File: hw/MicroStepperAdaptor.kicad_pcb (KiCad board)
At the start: 2 copper layers, 23 x 18 mm, 9 parts, among them P1 CONN_6, U1 QSBT40, U2 2_Phase_Motor

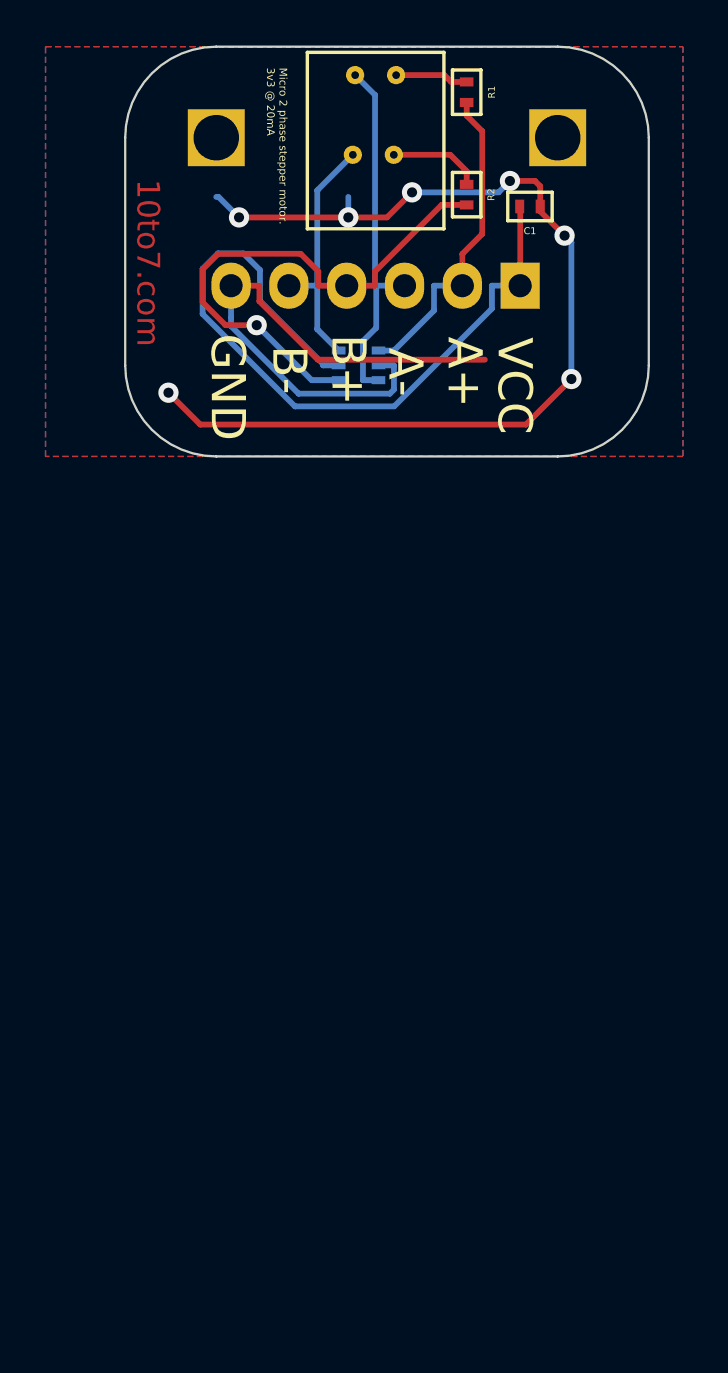
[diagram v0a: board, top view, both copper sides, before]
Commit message: revised stepper motor footprint and reduced the size of the board.
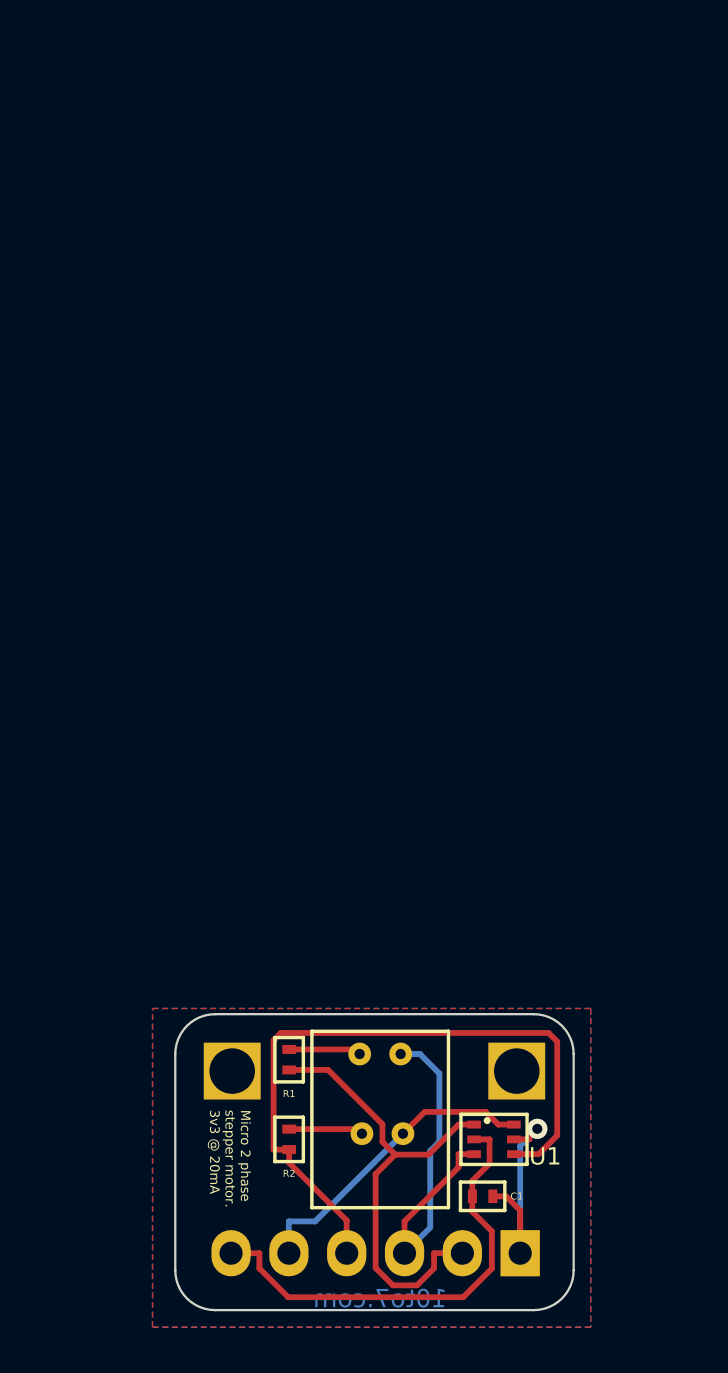
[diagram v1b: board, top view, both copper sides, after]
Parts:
- U1: moved to F.Cu
- U2: moved to B.Cu
- moved C1 43.5 mm to (146.7, 151.5), turned to 180 degrees
- moved 2mm_Pad_3 43.4 mm to (135.7, 146.0)
- moved R1 43.2 mm to (138.2, 145.5)
- moved 2mm_Pad_4 43.1 mm to (148.2, 146.0)
- moved U2 43.0 mm to (142.2, 147.0)
- moved 2mm_pad_2 42.5 mm to (151.5, 157.5)
- moved P1 42.5 mm to (142.0, 154.0)
- moved R2 42.2 mm to (138.2, 149.0)
- moved U1 34.5 mm to (147.2, 149.0)
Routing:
- net GND: track 69.4 -> 20.2 mm, vias 7 -> 0
- net VCC: track 33.0 -> 10.4 mm, vias 0 -> 1
- net /A+: track 14.2 -> 21.1 mm
- net /B+: track 23.5 -> 30.2 mm, vias 1 -> 0
- net /B-: track 10.9 -> 13.5 mm
- net Net-(R2-Pad2): track 4.08 -> 3.28 mm
- net /A-: track 16.0 -> 16.6 mm
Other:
- board size 23 x 18 mm -> 17.5 x 13 mm
- net class Default: clearance 0.254 -> 0
- rule trace_clearance: 0.254 -> 0
- board text added: "V0.2"
- board text removed: "V0.1"
